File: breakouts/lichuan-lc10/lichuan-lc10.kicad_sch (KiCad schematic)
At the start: 9 parts, among them J1 RJ45_LED_Shielded, J2 RJ45_LED_Shielded, J3 TERM-BLK-8H-S, J4 Conn_01x03, J5 Conn_01x02

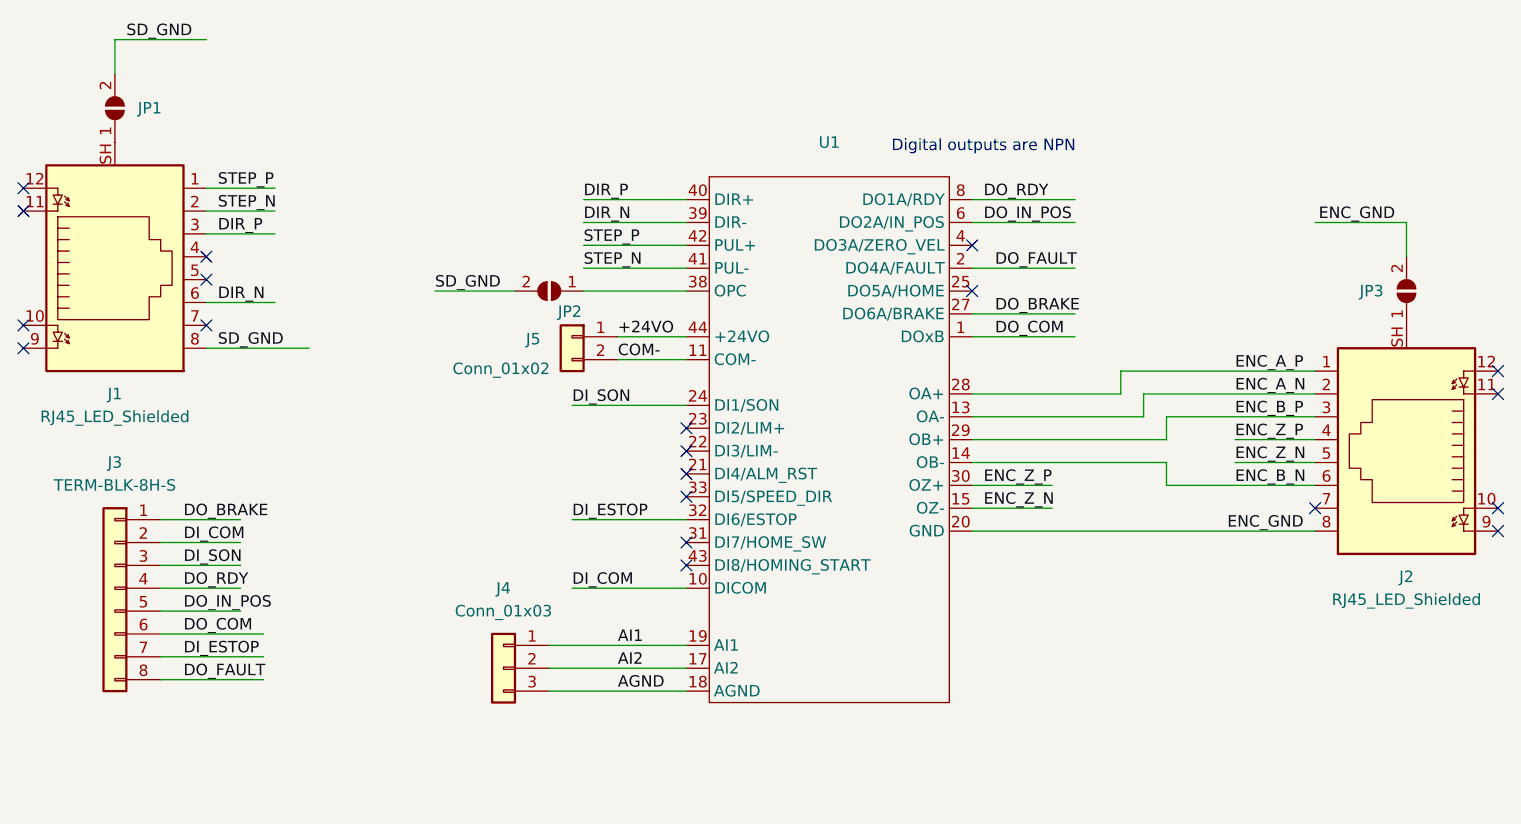
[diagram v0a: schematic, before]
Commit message: Fix ERC, add title information to sch, add initial version of build scripts
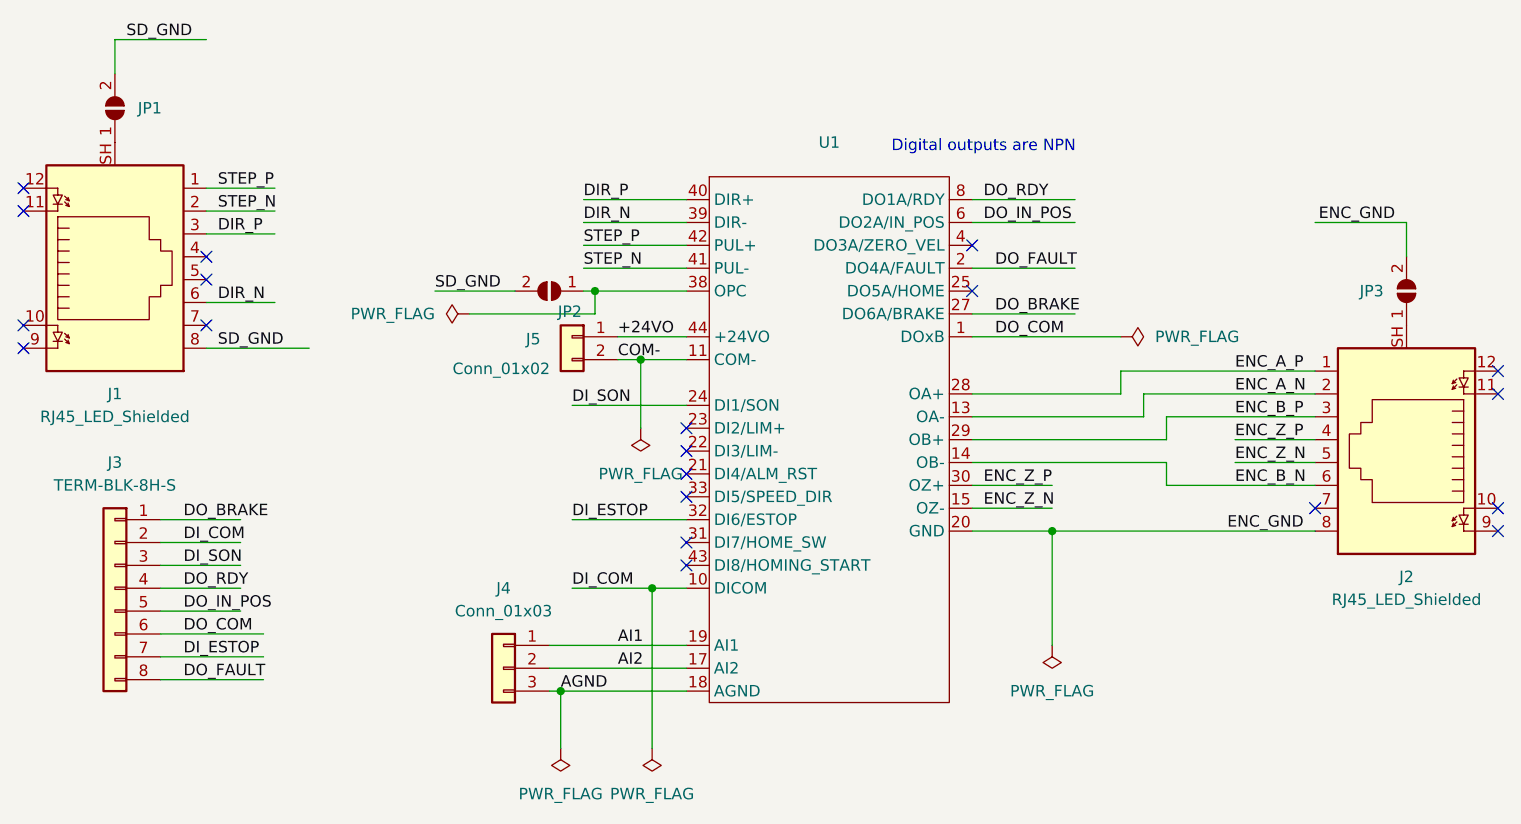
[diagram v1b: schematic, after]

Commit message: Fill in BOM (LCSC#)
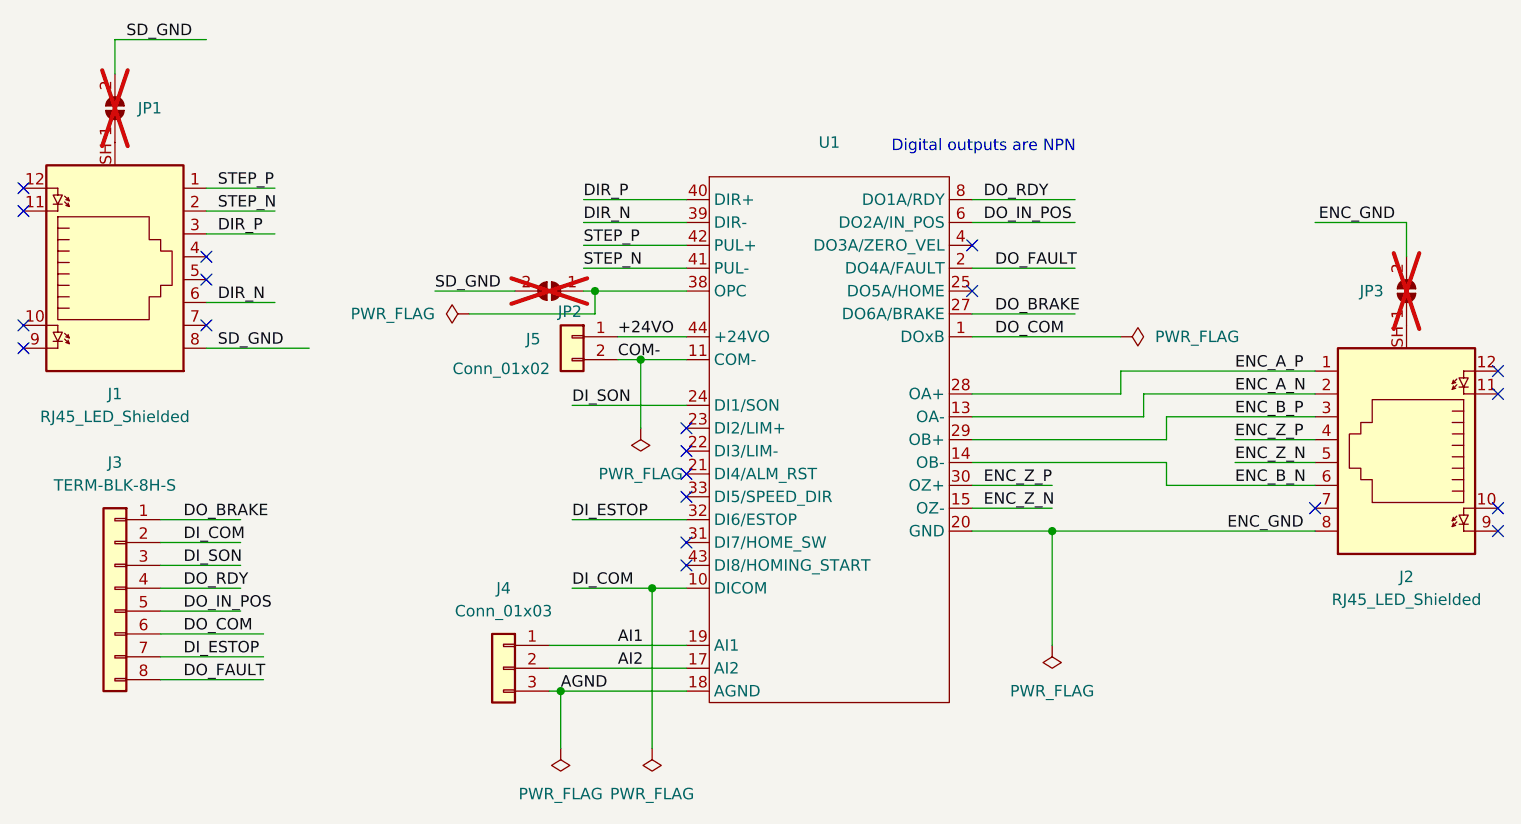
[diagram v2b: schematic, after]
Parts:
- JP1, JP2, JP3: now not fitted
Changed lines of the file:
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@@
 		(in_bom no)
 		(on_board yes)
-		(dnp no)
+		(dnp yes)
 		(fields_autoplaced yes)
 		(property "Reference" "JP1"
@@
 		(in_bom no)
 		(on_board yes)
-		(dnp no)
+		(dnp yes)
 		(fields_autoplaced yes)
 		(property "Reference" "JP3"
@@
 		(in_bom no)
 		(on_board yes)
-		(dnp no)
+		(dnp yes)
 		(property "Reference" "JP2"
 			(at 108.966 81.026 0)
